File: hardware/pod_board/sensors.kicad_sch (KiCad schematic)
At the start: 9 parts, among them J2 IMU (BNO085 breakout), J3 GNSS (NEO-M8N breakout), J4 Gesture puck (JST-GH), J5 SWD (ST-Link), J6 ELM327 fallback (USART3)

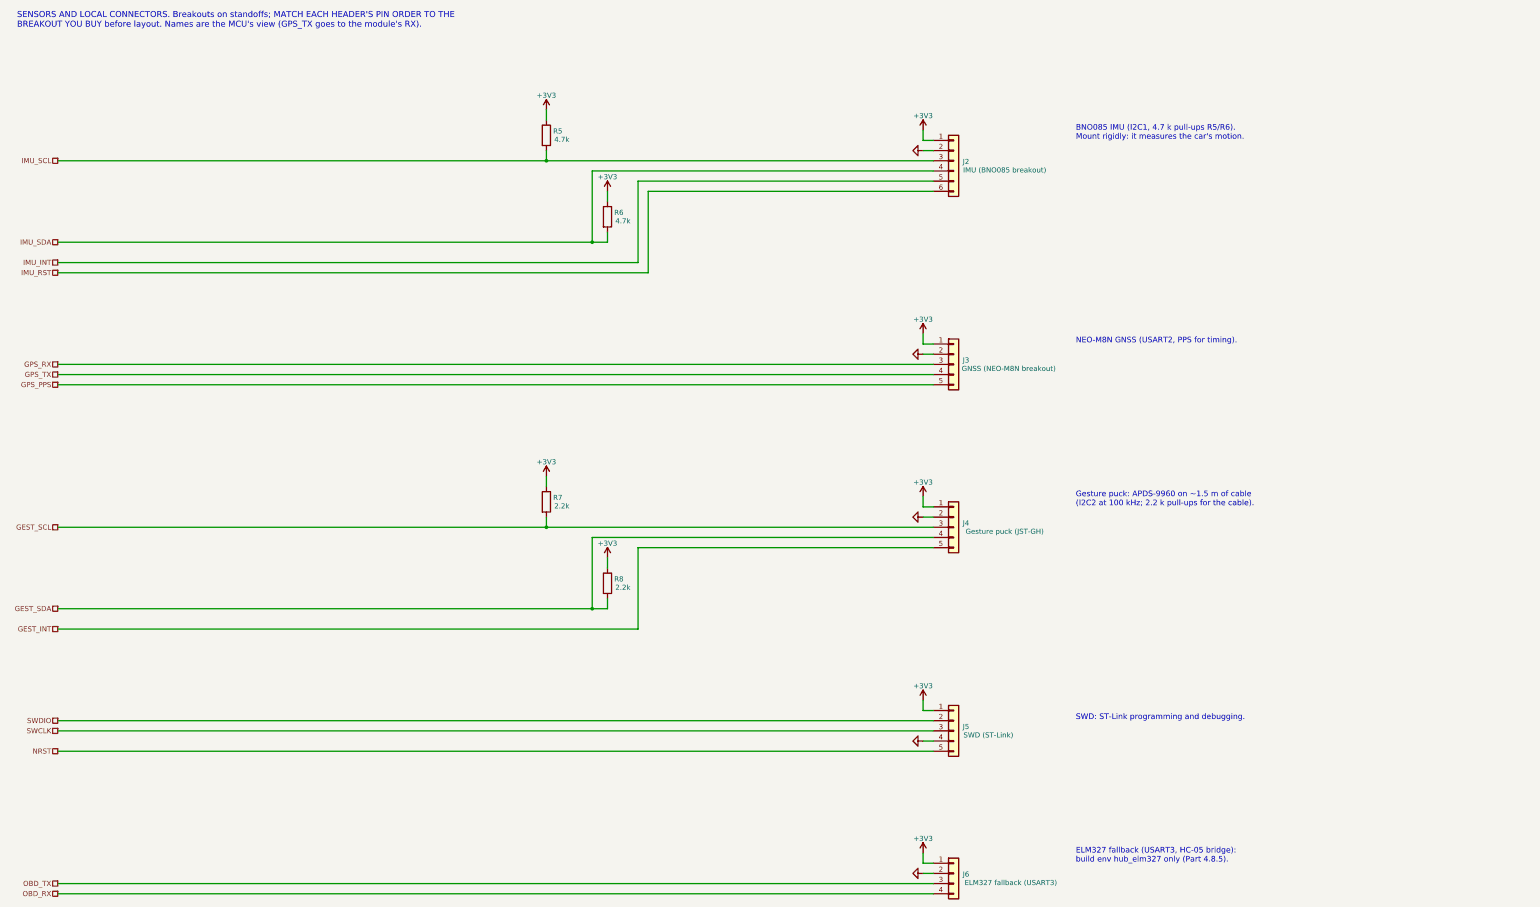
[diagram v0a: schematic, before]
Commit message: PCBs routed, labelled and ready to order: Rev 1 fabrication files and buy list
Both boards placed, routed and finished by script (hardware/gen): layout.sh places
(placement.py, with silkscreen names for every terminal, port, header and button),
route.sh routes with Freerouting inside rule areas and net classes from the layout
guide and keeps a board only with 0 DRC errors, 0 unconnected and exact schematic
parity, routespec.sh checks what the DRC cannot (planes, crystal, converter loop,
IPC-2221 widths), finish.sh adds the bottom-silkscreen identification and writes
the fabrication files (gerbers, drill, BOM, positions) only when the DRC passes.

- Pod 70 x 53 mm, 4 layers: In1 solid GND, In2 +3V3, 530 teardrops; no DRC warnings.
- Power 95 x 66 mm, 2 layers, 2 oz: 10 A rail as a zone, converter re-placed (switch
  node 16 mm, feedback 7 mm, no vias; was 78 mm and 40 mm), 328 teardrops.
- Screw terminals turned to open outward; RESET/BOOT side-push on the pod's left
  edge; USB-C footprint with a 3D model (GCT USB4105).
- Pod J2 now the Adafruit 4754's JP1 row pin for pin (the old order shorted its
  3.3 V output to ground); IMU reset on a new J8; HC-05 header fed 5 V.
- Buy list per footprint and module connections in bill-of-materials.md section 10.
- LAYOUT_GUIDE rewritten as how the boards were routed and how to review them;
  decisions, progress log and BUILD_GUIDE updated; power box follows the wider board.
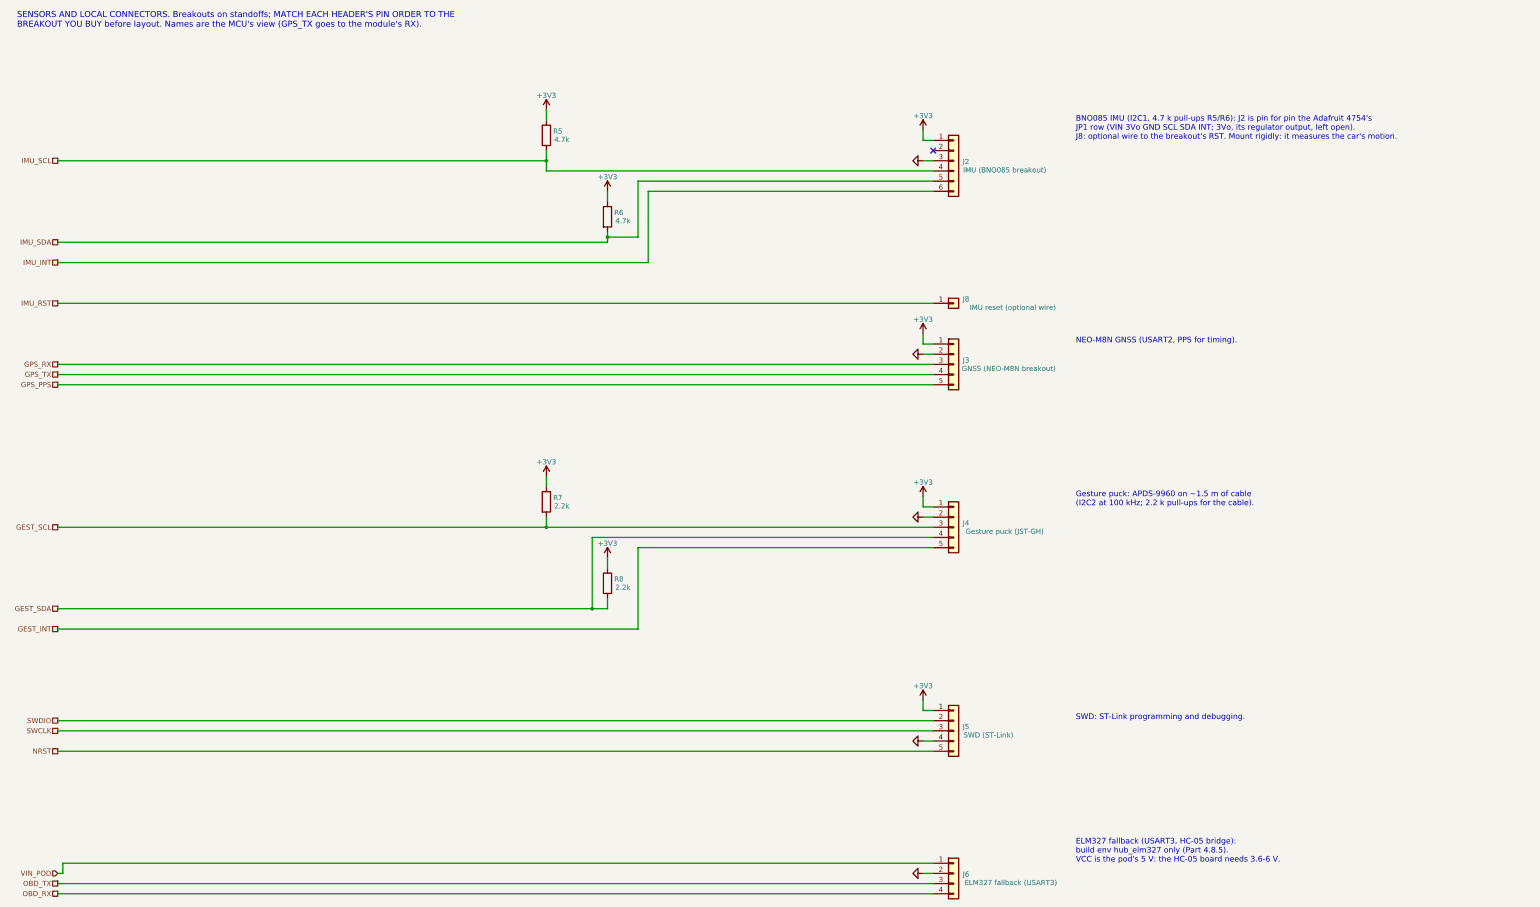
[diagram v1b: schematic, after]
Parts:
- added J8: IMU reset (optional wire), Connector_PinHeader_2.54mm:PinHeader_1x01_P2.54mm_Vertical, symbol Connector_Generic:Conn_01x01
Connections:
- net +3V3: no longer J6.1 (Pin_1)
- net GND: now also J2.3 (Pin_3); no longer J2.2 (Pin_2)
- net IMU_INT: now also J2.6 (Pin_6); no longer J2.5 (Pin_5)
- net IMU_RST: now also J8.1 (Pin_1); no longer J2.6 (Pin_6)
- net IMU_SCL: now also J2.4 (Pin_4); no longer J2.3 (Pin_3)
- net IMU_SDA: now also J2.5 (Pin_5); no longer J2.4 (Pin_4)
- new net VIN_POD: J6.1 (Pin_1)
- no-connect marks 0 -> 1
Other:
- note added: "BNO085 IMU (I2C1, 4.7 k pull-ups R5/R6): J2 is pin for pin the Adafruit 4754's JP1 row (VIN 3Vo GND SCL SDA INT; 3Vo, its regulator output, left open). J8: optional wire to the breakout's RST. Mount rigidly: it measures the car's motion."
- note added: "ELM327 fallback (USART3, HC-05 bridge): build env hub_elm327 only (Part 4.8.5). VCC is the pod's 5 V: the HC-05 board needs 3.6-6 V."
- note removed: "BNO085 IMU (I2C1, 4.7 k pull-ups R5/R6). Mount rigidly: it measures the car's motion."
- note removed: "ELM327 fallback (USART3, HC-05 bridge): build env hub_elm327 only (Part 4.8.5)."
